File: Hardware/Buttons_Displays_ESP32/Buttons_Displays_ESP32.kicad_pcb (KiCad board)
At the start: 2 copper layers, 28 parts, among them J1 1778612, J2 1778612, J3 1778612, J4 1778612, J5 i2c, J6 USB_C_Receptacle_USB2.0_16P, SW1 SW_Push, SW2 SW_Push, U1 ESP32-S3-WROOM-1, U2 USBLC6-2P6

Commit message: Update Buttons_Displays_ESP32.kicad_pcb
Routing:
- net GPIO6: track 71.3 -> 71.8 mm
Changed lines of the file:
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@@
 		(tags "Connector")
 		(property "Reference" "J3"
-			(at -5 0 0)
+			(at 0 0 0)
 			(layer "F.SilkS")
 			(effects
@@
 		(tags "Connector")
 		(property "Reference" "J4"
-			(at -2.75 4.5 0)
+			(at 0 0 0)
 			(layer "F.SilkS")
 			(effects
@@
 		(tags "Connector")
 		(property "Reference" "J1"
-			(at -3 -3.5 0)
+			(at 0 0 0)
 			(layer "F.SilkS")
 			(effects
@@
 			(net 38 "unconnected-(U1-IO6-Pad6)")
 			(pinfunction "IO6")
-			(pintype "bidirectional")
+			(pintype "bidirectional+no_connect")
 		)
 		(pad "7" smd rect
@@
 		(tags "Connector")
 		(property "Reference" "J2"
-			(at -0.83 -3.32 0)
+			(at 0 0 0)
 			(layer "F.SilkS")
 			(effects
@@
 		)
 		(fp_text user "${REFERENCE}"
-			(at -2.5 4.5 0)
+			(at 0 0 0)
 			(layer "F.Fab")
 			(effects
@@
 	)
 	(segment
-		(start 153.9 77.4)
-		(end 150.75 74.25)
+		(start 153.3 101.1)
+		(end 155 99.4)
 		(width 0.2)
 		(layer "F.Cu")
@@
 	)
 	(segment
-		(start 153.9 83.65)
-		(end 153.9 77.4)
+		(start 155 84.75)
+		(end 153.9 83.65)
 		(width 0.2)
 		(layer "F.Cu")
@@
 	)
 	(segment
-		(start 135.6 101.1)
-		(end 153.056677 101.1)
+		(start 126.25 91.75)
+		(end 135.6 101.1)
 		(width 0.2)
 		(layer "F.Cu")
@@
 	)
 	(segment
-		(start 155 84.75)
-		(end 153.9 83.65)
+		(start 153.9 83.65)
+		(end 153.9 77.4)
 		(width 0.2)
 		(layer "F.Cu")
@@
 	)
 	(segment
-		(start 155 99.156677)
+		(start 155 99.4)
 		(end 155 84.75)
 		(width 0.2)
@@
 	)
 	(segment
-		(start 153.056677 101.1)
-		(end 155 99.156677)
+		(start 135.6 101.1)
+		(end 153.3 101.1)
 		(width 0.2)
 		(layer "F.Cu")
@@
 	)
 	(segment
-		(start 148.17 73.92)
-		(end 145.25 73.92)
+		(start 153.9 77.4)
+		(end 150.75 74.25)
 		(width 0.2)
 		(layer "F.Cu")
@@
 	)
 	(segment
-		(start 126.25 91.75)
-		(end 135.6 101.1)
+		(start 148.17 73.92)
+		(end 145.25 73.92)
 		(width 0.2)
 		(layer "F.Cu")
@@
 	)
 	(segment
-		(start 153.222363 101.5)
-		(end 158 96.722363)
+		(start 148.4 72.65)
+		(end 145.25 72.65)
 		(width 0.2)
 		(layer "F.Cu")
@@
 	)
 	(segment
-		(start 158 79.5)
-		(end 151.25 72.75)
+		(start 133.8 101.8)
+		(end 153.4 101.8)
 		(width 0.2)
 		(layer "F.Cu")
@@
 	(segment
 		(start 131.75 99.75)
-		(end 133.5 101.5)
+		(end 133.8 101.8)
 		(width 0.2)
 		(layer "F.Cu")
@@
 	)
 	(segment
-		(start 148.4 72.65)
-		(end 145.25 72.65)
+		(start 153.4 101.8)
+		(end 158 97.2)
 		(width 0.2)
 		(layer "F.Cu")
@@
 	)
 	(segment
-		(start 133.5 101.5)
-		(end 153.222363 101.5)
+		(start 158 79.5)
+		(end 151.25 72.75)
 		(width 0.2)
 		(layer "F.Cu")
@@
 	)
 	(segment
-		(start 158 96.722363)
+		(start 158 97.2)
 		(end 158 79.5)
 		(width 0.2)

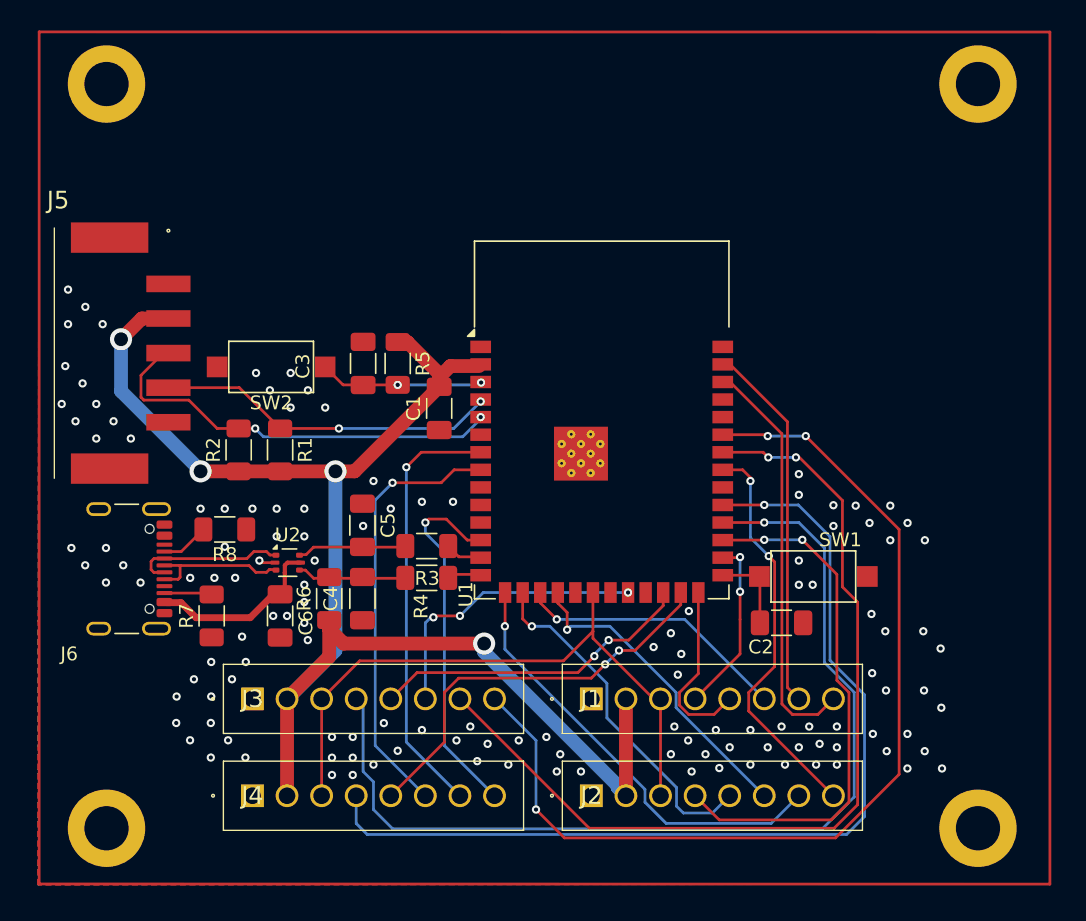
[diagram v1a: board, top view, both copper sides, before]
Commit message: Kut ipo ;)
IO pin voor tril motor toegevoegd
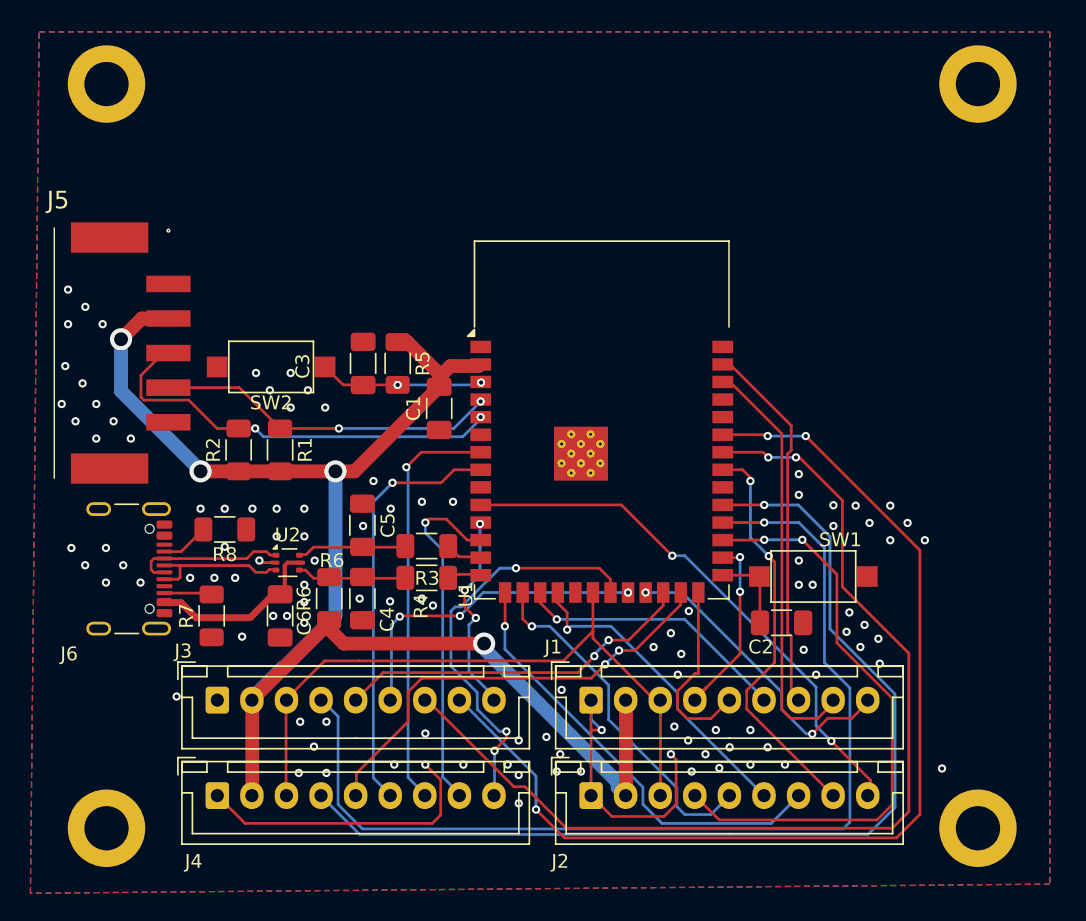
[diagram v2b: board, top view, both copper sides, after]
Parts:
- J1, J2, J3, J4: value 1778612 -> Conn_01x09; footprint ConnectorPT:1778612 -> Connector_JST:JST_XH_B9B-XH-A_1x09_P2.50mm_Vertical
- moved J3 2.54 mm to (108.7, 91.8)
- moved J4 2.54 mm to (108.7, 98.7)
- moved J1 0.09 mm to (135.7, 91.8)
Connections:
- U1 pad 10: unconnected-(U1-IO17-Pad10) -> VIB2
- U1 pad 11: unconnected-(U1-IO18-Pad11) -> VIB3
- U1 pad 21: unconnected-(U1-IO13-Pad21) -> VIB4
- U1 pad 23: unconnected-(U1-IO21-Pad23) -> VIB1
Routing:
- net GND: track 1.19 -> 43.6 mm, vias 133 -> 111
- net VIB2: track 0.00 -> 39.2 mm, vias 0 -> 2
- net VIB4: track 0.00 -> 29.9 mm, vias 0 -> 3
- net VIB1: track 0.00 -> 22.3 mm, vias 0 -> 2
- net VIB3: track 0.00 -> 14.6 mm, vias 0 -> 3
- net GPIO5: track 65.7 -> 73.6 mm
- net SCLK: track 45.6 -> 52.4 mm
- net RES2: track 38.5 -> 43.0 mm
- net GPIO6: track 71.8 -> 76.3 mm
- net RES4: track 69.6 -> 73.7 mm
- net DC3: track 23.3 -> 26.6 mm
- net RES3: track 71.8 -> 74.7 mm
- net DC4: track 29.7 -> 32.3 mm
- net CS/SS3: track 21.0 -> 23.5 mm
- net +3.3V: track 112.0 -> 114.2 mm
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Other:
- board text added: "C4"
- board text added: "R6"

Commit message: Update Buttons_Displays_ESP32.kicad_pcb
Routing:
- net GND: vias 111 -> 107
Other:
- board outline added: 70.5 x 61.8 mm
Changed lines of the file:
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@@
 		(tags "Connector")
 		(property "Reference" "J5"
-			(at -11.05 7.975 180)
+			(at -11.05 6.925 180)
 			(layer "F.SilkS")
 			(effects
@@
 		)
 	)
+	(gr_rect
+		(start 97.25 43.25)
+		(end 167.75 105)
+		(stroke
+			(width 0.05)
+			(type default)
+		)
+		(fill none)
+		(layer "Edge.Cuts")
+	)
 	(gr_text "C4\n"
 		(at 121 86 90)
@@
 	)
 	(via
-		(at 97.92 62.16)
-		(size 0.6)
-		(drill 0.3)
-		(layers "F.Cu" "B.Cu")
-		(free yes)
-		(net 2)
-	)
-	(via
 		(at 120 76)
 		(size 0.6)
@@
 	)
 	(via
-		(at 97.72 67.69)
-		(size 0.6)
-		(drill 0.3)
-		(layers "F.Cu" "B.Cu")
-		(free yes)
-		(net 2)
-	)
-	(via
 		(at 149.75 96.5)
 		(size 0.6)
@@
 	)
 	(via
-		(at 97.92 64.66)
-		(size 0.6)
-		(drill 0.3)
-		(layers "F.Cu" "B.Cu")
-		(free yes)
-		(net 2)
-	)
-	(via
 		(at 143 97)
 		(size 0.6)
@@
 	)
 	(via
-		(at 97.46 70.43)
-		(size 0.6)
-		(drill 0.3)
-		(layers "F.Cu" "B.Cu")
-		(free yes)
-		(net 2)
-	)
-	(via
 		(at 150.75 83.5)
 		(size 0.6)
@@
 		(polygon
 			(pts
-				(xy 168.900024 43.54) (xy 168.900024 105.14) (xy 95.2 105.8) (xy 95.83 43.53)
+				(xy 169.5 43.5) (xy 169.5 105) (xy 95 105) (xy 95 43.5)
 			)
 		)

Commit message: laatste aanpassingen
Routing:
- net GND: vias 107 -> 108
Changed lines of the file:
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@@
+	)
+	(via
+		(at 121 93.5)
+		(size 0.6)
+		(drill 0.3)
+		(layers "F.Cu" "B.Cu")
+		(free yes)
+		(net 2)
 	)
 	(via
@@
 	)
 	(segment
-		(start 155.94 97.64)
-		(end 155.94 98.77)
+		(start 155.73 97.43)
+		(end 155.73 98.74)
+		(width 0.2)
+		(layer "F.Cu")
+		(net 46)
+	)
+	(segment
+		(start 153.1 94.8)
+		(end 155.73 97.43)
 		(width 0.2)
 		(layer "F.Cu")
@@
 		(width 0.2)
 		(layer "F.Cu")
-		(net 46)
-	)
-	(segment
-		(start 153.1 94.8)
-		(end 155.94 97.64)
-		(width 0.2)
-		(layer "F.Cu")
